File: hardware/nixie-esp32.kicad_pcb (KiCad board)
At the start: 2 copper layers, 52 parts, among them IC1 MCP1661T-E_OT, IC2 CD4504BM, J1 USB4216-03-A_REVA, SW1 RESET, SW2 BOOT, U1 AP7361C-33E-13, U2 ESP32-S3-WROOM-1, U3 SN74AHCT1G125DBVR, U4 HV5622PG

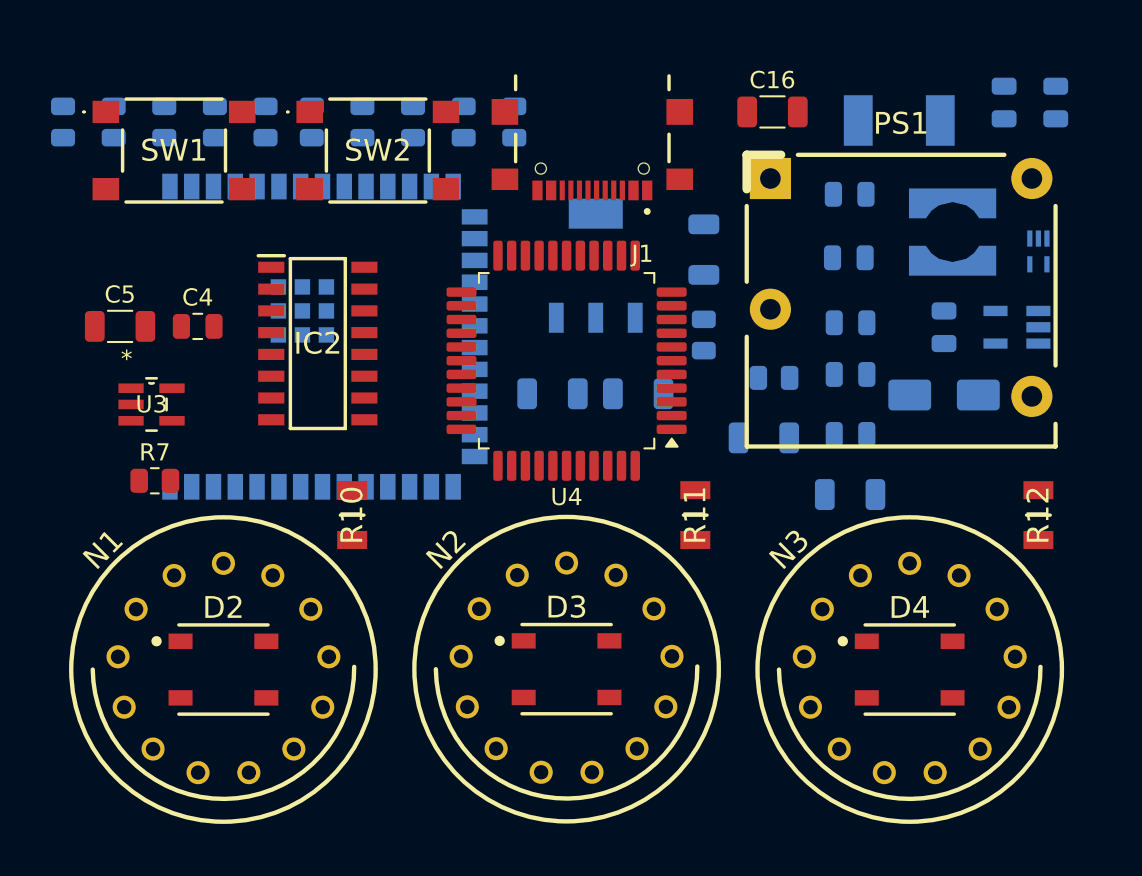
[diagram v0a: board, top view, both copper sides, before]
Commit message: Refine PCB component placement
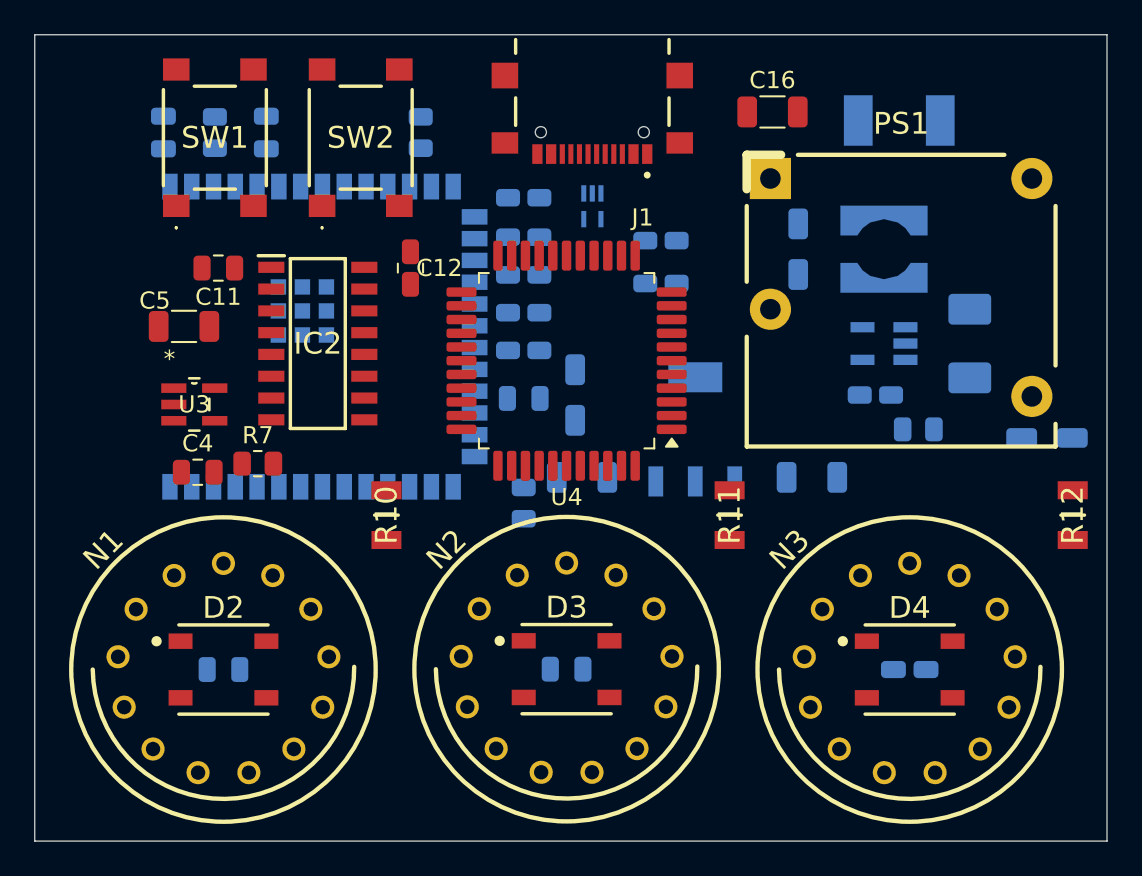
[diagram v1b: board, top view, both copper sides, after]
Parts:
- C11, C12: moved to F.Cu
- moved C3 49.0 mm to (128.0, 82.2), turned to 90 degrees
- moved C15 46.0 mm to (134.0, 82.2), turned to 90 degrees
- moved C6 45.8 mm to (131.5, 113.5), turned to 0 degrees
- moved C11 37.0 mm to (131.2, 90.1), turned to 0 degrees
- moved R1 35.5 mm to (157.0, 88.5), turned to 0 degrees
- moved R2 33.3 mm to (157.0, 91.0), turned to 0 degrees
- moved C7 29.1 mm to (151.5, 113.5), turned to 0 degrees
- moved C12 26.4 mm to (142.4, 90.1), turned to 90 degrees
- moved D1 26.1 mm to (153.0, 86.5)
- moved R6 25.4 mm to (149.0, 103.8), turned to 90 degrees
- moved C9 22.8 mm to (179.5, 100.0), turned to 180 degrees
- moved C8 20.1 mm to (171.5, 113.5), turned to 0 degrees
- moved C13 19.2 mm to (149.0, 97.7), turned to 0 degrees
- moved R4 18.5 mm to (149.0, 86.0), turned to 0 degrees
- moved C14 17.0 mm to (152.0, 97.5), turned to 90 degrees
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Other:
- board outline added: 62.5 x 47 mm

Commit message: Apply second placement audit: boost cluster, R12 edge margin, mounting holes
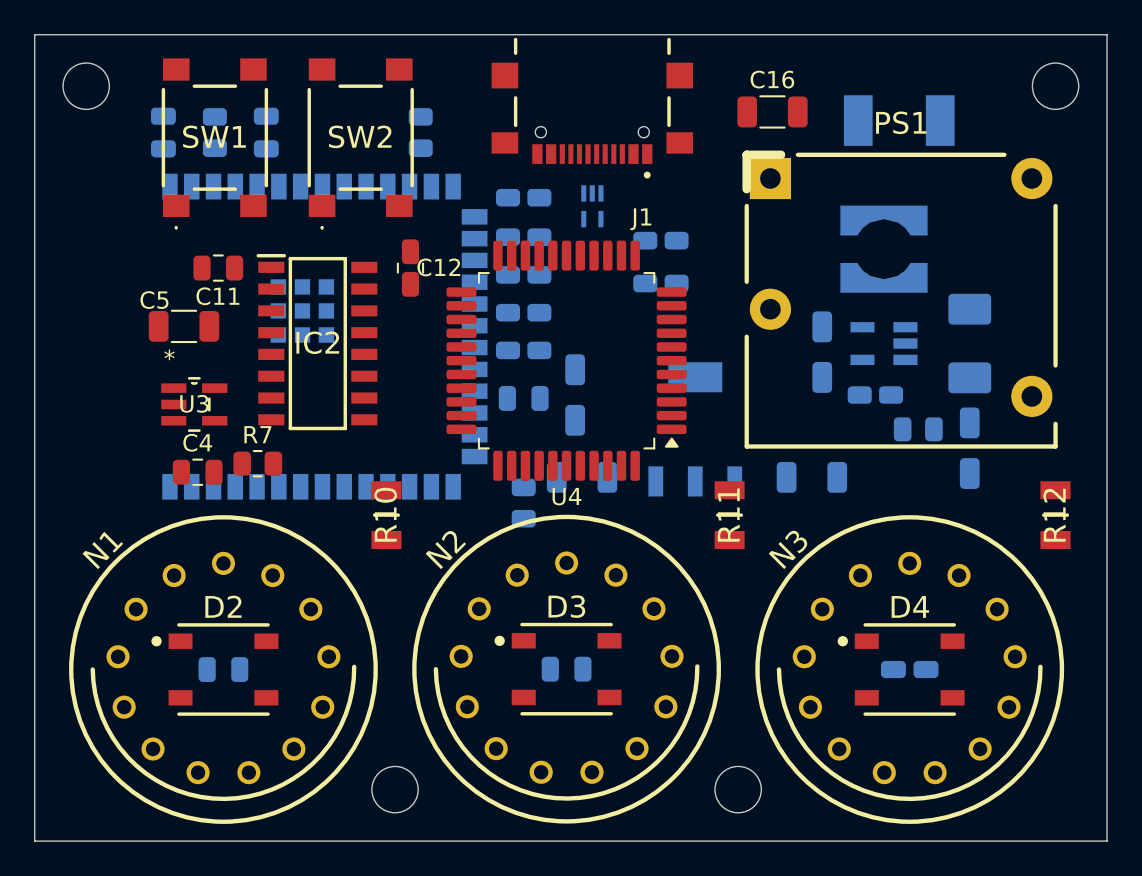
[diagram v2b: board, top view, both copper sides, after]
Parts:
- added H1: MountingHole_2.7mm_M2.5, MountingHole_2.7mm_M2.5, F.Cu at (123.5, 79.5)
- added H2: MountingHole_2.7mm_M2.5, MountingHole_2.7mm_M2.5, F.Cu at (180.0, 79.5)
- added H3: MountingHole_2.7mm_M2.5, MountingHole_2.7mm_M2.5, F.Cu at (141.5, 120.5)
- added H4: MountingHole_2.7mm_M2.5, MountingHole_2.7mm_M2.5, F.Cu at (161.5, 120.5)
- moved C10 6.16 mm to (166.4, 95.0)
- moved C9 4.54 mm to (175.0, 100.6), turned to 90 degrees
- moved R12 1.00 mm to (180.0, 104.5)

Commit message: .
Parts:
- moved R12 1.00 mm to (179.0, 104.5)
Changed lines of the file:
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@@
 	(footprint "nixie-esp32:RESC3116X65N"
 		(layer "F.Cu")
-		(at 180 104.5 90)
+		(at 179 104.5 90)
 		(descr "CRGH1206")
 		(tags "Resistor")

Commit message: Set LED labels
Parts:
- renumbered D2 to LED1, D3 to LED2, D4 to LED3
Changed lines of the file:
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@@
 		(descr "Bivar SMTLA5050RGB addressable RGB LED, 5.0 x 5.4 x 1.6 mm PLCC4, datasheet recommended land pattern")
 		(tags "Bivar SMTLA5050RGB addressable RGB LED 5050 PLCC4")
-		(property "Reference" "D2"
+		(property "Reference" "LED1"
 			(at 0 -3.6 0)
 			(layer "F.SilkS")
@@
 		(descr "Bivar SMTLA5050RGB addressable RGB LED, 5.0 x 5.4 x 1.6 mm PLCC4, datasheet recommended land pattern")
 		(tags "Bivar SMTLA5050RGB addressable RGB LED 5050 PLCC4")
-		(property "Reference" "D4"
+		(property "Reference" "LED3"
 			(at 0 -3.6 0)
 			(layer "F.SilkS")
@@
 		(descr "Bivar SMTLA5050RGB addressable RGB LED, 5.0 x 5.4 x 1.6 mm PLCC4, datasheet recommended land pattern")
 		(tags "Bivar SMTLA5050RGB addressable RGB LED 5050 PLCC4")
-		(property "Reference" "D3"
+		(property "Reference" "LED2"
 			(at 0 -3.6 0)
 			(layer "F.SilkS")

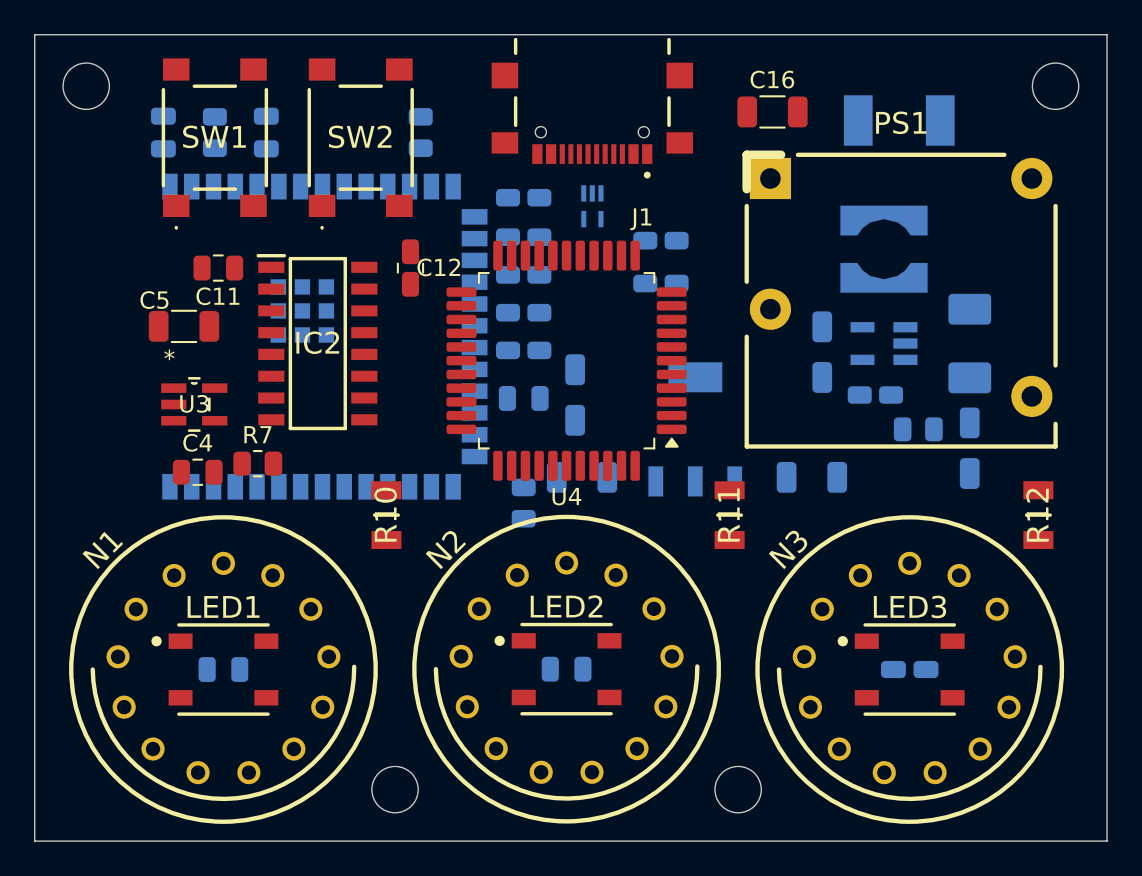
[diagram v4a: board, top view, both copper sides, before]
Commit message: Silkscreen pass: tidy reference labels, add board name/rev/date
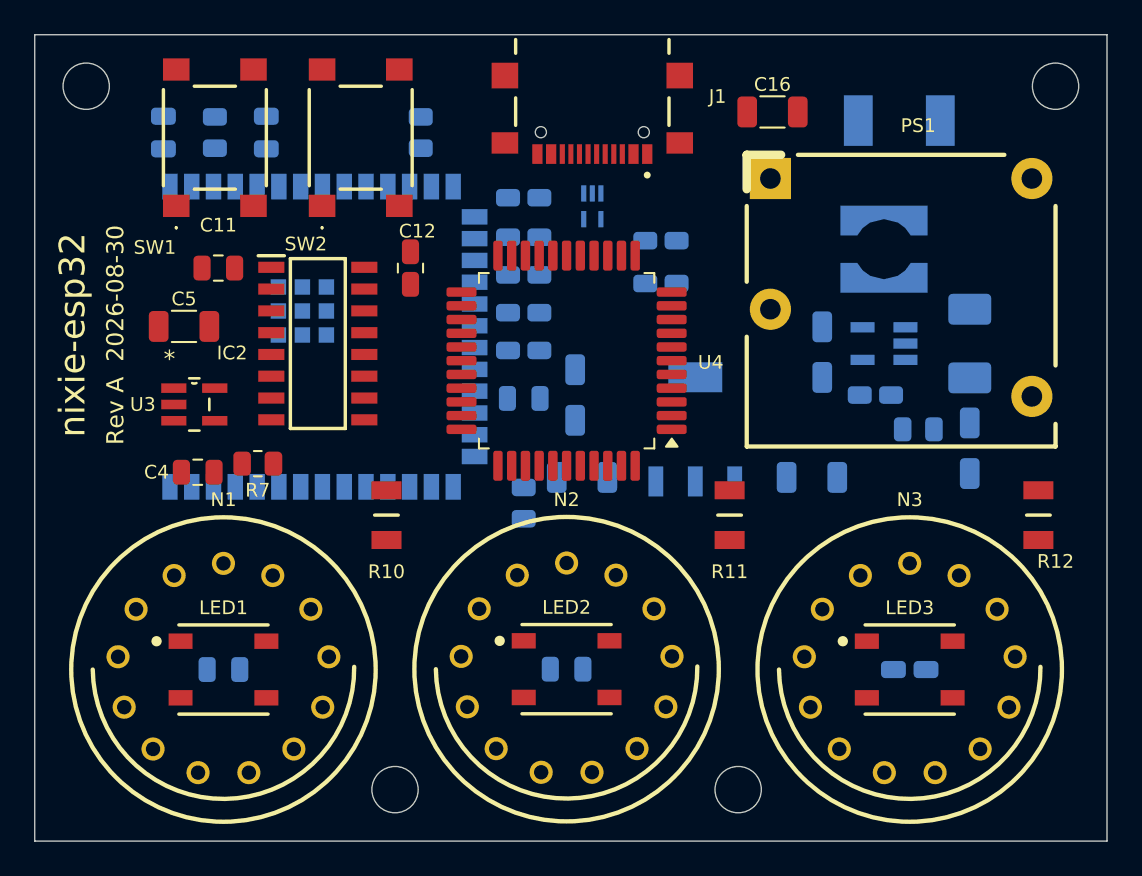
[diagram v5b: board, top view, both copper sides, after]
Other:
- board text added: "Rev A 2026-08-30"
- board text added: "nixie-esp32"
